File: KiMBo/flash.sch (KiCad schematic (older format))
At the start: 1 part

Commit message: Add eMMC to the schematic
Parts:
- removed U?: S25FL256SAGNFI001, symbol S25FL256SAGNFI001
- added C? (x7): CP1, symbol CP1
- added R? (x11): R, symbol R
- added U?: EMMC**G-S100, symbol EMMC**G-S100
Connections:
- net labels added: +3V3, GND, MMC1_CLK, MMC1_CMD, MMC1_DAT0, MMC1_DAT1, MMC1_DAT2, MMC1_DAT3, MMC1_DAT4, MMC1_DAT5, MMC1_DAT6, MMC1_DAT7, MMC1_RSTN
- wire segments 0 -> 127
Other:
- note removed: "Use 512MB NOR Flash ?"

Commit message: Add 153-Pin BGA eMMC footprint
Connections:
- wire segments 127 -> 76
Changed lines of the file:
@@
 $EndComp
 Wire Wire Line
-	7350 3750 7350 4450
-Wire Wire Line
-	7350 4450 7350 4550
-Wire Wire Line
-	7350 4550 7350 4650
-Wire Wire Line
-	7350 4650 7350 4750
-Wire Wire Line
-	7350 3750 7950 3750
-Wire Wire Line
-	7950 3750 8050 3750
-Wire Wire Line
-	8050 3750 8150 3750
-Wire Wire Line
-	8150 3750 8250 3750
-Wire Wire Line
-	8250 3750 8350 3750
-Wire Wire Line
-	8350 3750 9600 3750
-Wire Wire Line
-	9600 3750 9850 3750
-Wire Wire Line
-	9850 3750 10100 3750
-Wire Wire Line
-	10100 3750 10350 3750
-Wire Wire Line
-	10350 3750 10600 3750
-Wire Wire Line
-	10600 3750 10850 3750
-Wire Wire Line
-	10850 3750 11100 3750
-Wire Wire Line
-	11100 3750 11350 3750
-Wire Wire Line
-	11350 3750 11600 3750
-Wire Wire Line
-	11600 3750 11850 3750
-Wire Wire Line
-	11850 3750 12100 3750
+	7350 3750 7350 4750
+Wire Wire Line
+	7350 3750 12100 3750
 Wire Wire Line
 	7400 4450 7350 4450
@@
 	8350 3750 8350 3800
 Wire Wire Line
-	7350 4900 7350 5000
-Wire Wire Line
-	7350 5000 7350 5100
-Wire Wire Line
-	7350 5100 7350 5200
-Wire Wire Line
-	7350 5200 7350 5900
-Wire Wire Line
-	7350 5900 7350 5950
-Wire Wire Line
-	5850 5900 6150 5900
-Wire Wire Line
-	6150 5900 6450 5900
-Wire Wire Line
-	6450 5900 6750 5900
-Wire Wire Line
-	6750 5900 7050 5900
-Wire Wire Line
-	7050 5900 7350 5900
-Wire Wire Line
-	7350 5900 7950 5900
-Wire Wire Line
-	7950 5900 8050 5900
-Wire Wire Line
-	8050 5900 8150 5900
-Wire Wire Line
-	8150 5900 8250 5900
-Wire Wire Line
-	8250 5900 8350 5900
-Wire Wire Line
-	8350 5900 9000 5900
-Wire Wire Line
-	9000 5900 9400 5900
-Wire Wire Line
-	5850 4900 6150 4900
-Wire Wire Line
-	6150 4900 6450 4900
-Wire Wire Line
-	6450 4900 6750 4900
-Wire Wire Line
-	6750 4900 7050 4900
-Wire Wire Line
-	7050 4900 7350 4900
-Wire Wire Line
-	7350 4900 7400 4900
+	7350 4900 7350 5950
+Wire Wire Line
+	5850 5900 9400 5900
+Wire Wire Line
+	5850 4900 7400 4900
 Wire Wire Line
 	7400 5000 7350 5000
@@
 $EndComp
 Wire Wire Line
-	8950 4200 9600 4200
-Wire Wire Line
-	9600 4200 12200 4200
+	8950 4200 12200 4200
 Wire Wire Line
 	9600 4200 9600 4150
@@
 $EndComp
 Wire Wire Line
-	8950 4300 9850 4300
-Wire Wire Line
-	9850 4300 12200 4300
+	8950 4300 12200 4300
 Wire Wire Line
 	9850 4300 9850 4150
 Wire Wire Line
-	8950 4400 10100 4400
-Wire Wire Line
-	10100 4400 12200 4400
+	8950 4400 12200 4400
 Wire Wire Line
 	10100 4400 10100 4150
 Wire Wire Line
-	8950 4500 10350 4500
-Wire Wire Line
-	10350 4500 12200 4500
+	8950 4500 12200 4500
 Wire Wire Line
 	10350 4500 10350 4150
 Wire Wire Line
-	8950 4600 10600 4600
-Wire Wire Line
-	10600 4600 12200 4600
+	8950 4600 12200 4600
 Wire Wire Line
 	10600 4600 10600 4150
 Wire Wire Line
-	8950 4700 10850 4700
-Wire Wire Line
-	10850 4700 12200 4700
+	8950 4700 12200 4700
 Wire Wire Line
 	10850 4700 10850 4150
 Wire Wire Line
-	8950 4800 11100 4800
-Wire Wire Line
-	11100 4800 12200 4800
+	8950 4800 12200 4800
 Wire Wire Line
 	11100 4800 11100 4150
 Wire Wire Line
-	8950 4900 11350 4900
-Wire Wire Line
-	11350 4900 12200 4900
+	8950 4900 12200 4900
 Wire Wire Line
 	11350 4900 11350 4150
 Wire Wire Line
-	9000 5000 11600 5000
-Wire Wire Line
-	11600 5000 12200 5000
+	9000 5000 12200 5000
 Wire Wire Line
 	11600 5000 11600 4150
@@
 Connection ~ 8350 3750
 Wire Wire Line
-	9600 3700 9600 3750
-Wire Wire Line
-	9600 3750 9600 3850
+	9600 3700 9600 3850
 Connection ~ 9600 3750
 Wire Wire Line
@@
 	9000 5500 9000 5450
 Wire Wire Line
-	8950 5450 9000 5450
-Wire Wire Line
-	9000 5450 9400 5450
+	8950 5450 9400 5450
 Wire Wire Line
 	9400 5450 9400 5500
@@
 	9000 5150 9000 5100
 Wire Wire Line
-	9000 5100 11850 5100
-Wire Wire Line
-	11850 5100 12200 5100
+	9000 5100 12200 5100
 Wire Wire Line
 	8950 5300 9000 5300
@@
 	9000 5300 9000 5200
 Wire Wire Line
-	9000 5200 12100 5200
-Wire Wire Line
-	12100 5200 12200 5200
+	9000 5200 12200 5200
 Wire Wire Line
 	12100 5200 12100 4150

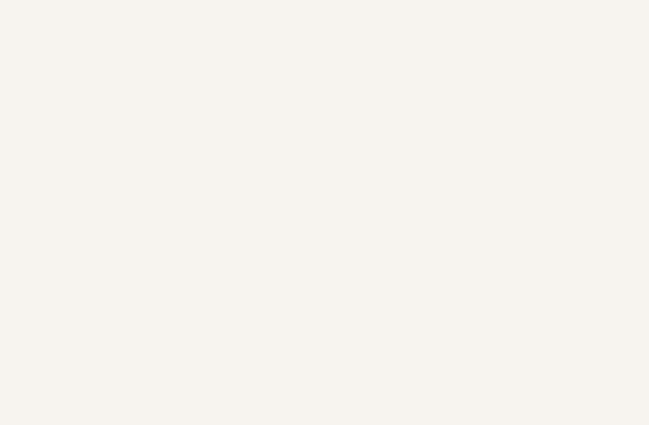
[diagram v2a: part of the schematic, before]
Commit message: Update schematic module file names, add HDMI module and SD module
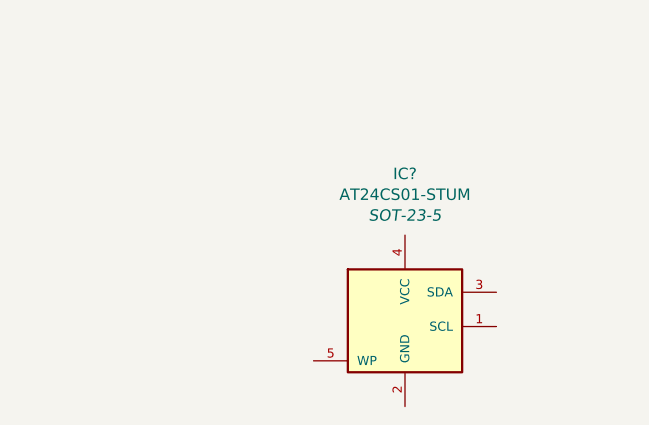
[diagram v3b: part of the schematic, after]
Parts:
- added IC?: AT24CS01-STUM, SOT-23-5, symbol AT24CS01-STUM
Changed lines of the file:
@@
 $Descr A3 16535 11693
 encoding utf-8
-Sheet 6 18
+Sheet 6 20
 Title ""
 Date ""
@@
 $EndDescr
 $Comp
-L +3V3 #PWR?
+L +3V3 #PWR081
 U 1 1 58938D4F
 P 9600 3700
-F 0 "#PWR?" H 9600 3550 50  0001 C CNN
+F 0 "#PWR081" H 9600 3550 50  0001 C CNN
 F 1 "+3V3" H 9615 3873 50  0000 C CNN
 F 2 "" H 9600 3700 50  0000 C CNN
@@
 Connection ~ 11850 3750
 $Comp
-L GND #PWR?
+L GND #PWR082
 U 1 1 5893C2D6
 P 7350 5950
-F 0 "#PWR?" H 7350 5700 50  0001 C CNN
+F 0 "#PWR082" H 7350 5700 50  0001 C CNN
 F 1 "GND" H 7355 5777 50  0000 C CNN
 F 2 "" H 7350 5950 50  0000 C CNN
@@
 Text Label 9550 5200 2    60   ~ 0
 MMC1_RSTN
+$Comp
+L AT24CS01-STUM IC?
+U 1 1 5895A97E
+P 11300 7500
+F 0 "IC?" H 11300 8118 50  0000 C CNN
+F 1 "AT24CS01-STUM" H 11300 8027 50  0000 C CNN
+F 2 "SOT-23-5" H 11300 7936 50  0000 C CIN
+F 3 "" H 11300 7500 50  0000 C CNN
+	1    11300 7500
+	1    0    0    -1
+$EndComp
 $EndSCHEMATC

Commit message: More progress made on the HDMI module
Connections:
- wire segments 76 -> 127
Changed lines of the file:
@@
 $EndComp
 Wire Wire Line
-	7350 3750 7350 4750
-Wire Wire Line
-	7350 3750 12100 3750
+	7350 3750 7350 4450
+Wire Wire Line
+	7350 4450 7350 4550
+Wire Wire Line
+	7350 4550 7350 4650
+Wire Wire Line
+	7350 4650 7350 4750
+Wire Wire Line
+	7350 3750 7950 3750
+Wire Wire Line
+	7950 3750 8050 3750
+Wire Wire Line
+	8050 3750 8150 3750
+Wire Wire Line
+	8150 3750 8250 3750
+Wire Wire Line
+	8250 3750 8350 3750
+Wire Wire Line
+	8350 3750 9600 3750
+Wire Wire Line
+	9600 3750 9850 3750
+Wire Wire Line
+	9850 3750 10100 3750
+Wire Wire Line
+	10100 3750 10350 3750
+Wire Wire Line
+	10350 3750 10600 3750
+Wire Wire Line
+	10600 3750 10850 3750
+Wire Wire Line
+	10850 3750 11100 3750
+Wire Wire Line
+	11100 3750 11350 3750
+Wire Wire Line
+	11350 3750 11600 3750
+Wire Wire Line
+	11600 3750 11850 3750
+Wire Wire Line
+	11850 3750 12100 3750
 Wire Wire Line
 	7400 4450 7350 4450
@@
 	8350 3750 8350 3800
 Wire Wire Line
-	7350 4900 7350 5950
-Wire Wire Line
-	5850 5900 9400 5900
-Wire Wire Line
-	5850 4900 7400 4900
+	7350 4900 7350 5000
+Wire Wire Line
+	7350 5000 7350 5100
+Wire Wire Line
+	7350 5100 7350 5200
+Wire Wire Line
+	7350 5200 7350 5900
+Wire Wire Line
+	7350 5900 7350 5950
+Wire Wire Line
+	5850 5900 6150 5900
+Wire Wire Line
+	6150 5900 6450 5900
+Wire Wire Line
+	6450 5900 6750 5900
+Wire Wire Line
+	6750 5900 7050 5900
+Wire Wire Line
+	7050 5900 7350 5900
+Wire Wire Line
+	7350 5900 7950 5900
+Wire Wire Line
+	7950 5900 8050 5900
+Wire Wire Line
+	8050 5900 8150 5900
+Wire Wire Line
+	8150 5900 8250 5900
+Wire Wire Line
+	8250 5900 8350 5900
+Wire Wire Line
+	8350 5900 9000 5900
+Wire Wire Line
+	9000 5900 9400 5900
+Wire Wire Line
+	5850 4900 6150 4900
+Wire Wire Line
+	6150 4900 6450 4900
+Wire Wire Line
+	6450 4900 6750 4900
+Wire Wire Line
+	6750 4900 7050 4900
+Wire Wire Line
+	7050 4900 7350 4900
+Wire Wire Line
+	7350 4900 7400 4900
 Wire Wire Line
 	7400 5000 7350 5000
@@
 $EndComp
 Wire Wire Line
-	8950 4200 12200 4200
+	8950 4200 9600 4200
+Wire Wire Line
+	9600 4200 12200 4200
 Wire Wire Line
 	9600 4200 9600 4150
@@
 $EndComp
 Wire Wire Line
-	8950 4300 12200 4300
+	8950 4300 9850 4300
+Wire Wire Line
+	9850 4300 12200 4300
 Wire Wire Line
 	9850 4300 9850 4150
 Wire Wire Line
-	8950 4400 12200 4400
+	8950 4400 10100 4400
+Wire Wire Line
+	10100 4400 12200 4400
 Wire Wire Line
 	10100 4400 10100 4150
 Wire Wire Line
-	8950 4500 12200 4500
+	8950 4500 10350 4500
+Wire Wire Line
+	10350 4500 12200 4500
 Wire Wire Line
 	10350 4500 10350 4150
 Wire Wire Line
-	8950 4600 12200 4600
+	8950 4600 10600 4600
+Wire Wire Line
+	10600 4600 12200 4600
 Wire Wire Line
 	10600 4600 10600 4150
 Wire Wire Line
-	8950 4700 12200 4700
+	8950 4700 10850 4700
+Wire Wire Line
+	10850 4700 12200 4700
 Wire Wire Line
 	10850 4700 10850 4150
 Wire Wire Line
-	8950 4800 12200 4800
+	8950 4800 11100 4800
+Wire Wire Line
+	11100 4800 12200 4800
 Wire Wire Line
 	11100 4800 11100 4150
 Wire Wire Line
-	8950 4900 12200 4900
+	8950 4900 11350 4900
+Wire Wire Line
+	11350 4900 12200 4900
 Wire Wire Line
 	11350 4900 11350 4150
 Wire Wire Line
-	9000 5000 12200 5000
+	9000 5000 11600 5000
+Wire Wire Line
+	11600 5000 12200 5000
 Wire Wire Line
 	11600 5000 11600 4150
@@
 Connection ~ 8350 3750
 Wire Wire Line
-	9600 3700 9600 3850
+	9600 3700 9600 3750
+Wire Wire Line
+	9600 3750 9600 3850
 Connection ~ 9600 3750
 Wire Wire Line
@@
 	9000 5500 9000 5450
 Wire Wire Line
-	8950 5450 9400 5450
+	8950 5450 9000 5450
+Wire Wire Line
+	9000 5450 9400 5450
 Wire Wire Line
 	9400 5450 9400 5500
@@
 	9000 5150 9000 5100
 Wire Wire Line
-	9000 5100 12200 5100
+	9000 5100 11850 5100
+Wire Wire Line
+	11850 5100 12200 5100
 Wire Wire Line
 	8950 5300 9000 5300
@@
 	9000 5300 9000 5200
 Wire Wire Line
-	9000 5200 12200 5200
+	9000 5200 12100 5200
+Wire Wire Line
+	12100 5200 12200 5200
 Wire Wire Line
 	12100 5200 12100 4150
